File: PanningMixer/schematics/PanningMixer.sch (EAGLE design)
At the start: 67 parts, among them IC1 NE5532D, IC2 NE5532D, IC4 TL047, Q1 BSS84, Q2 BSS123, X1 1503_02

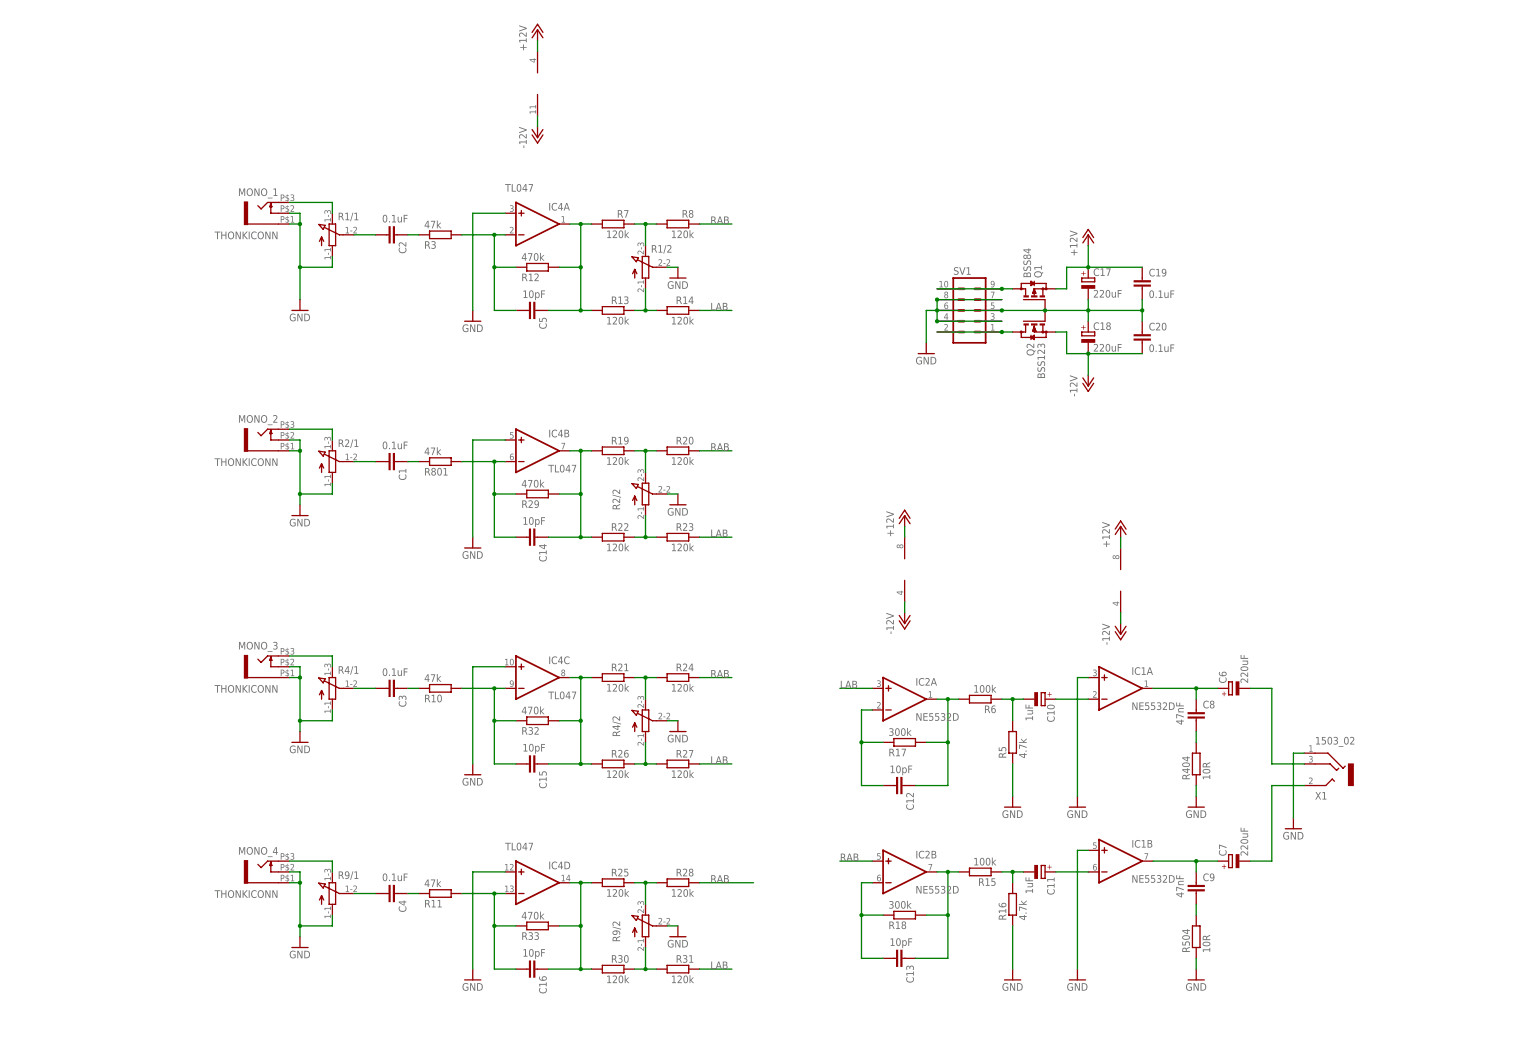
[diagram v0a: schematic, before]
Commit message: Completed placement of components and layout of PCB with no tracking. Added new stereo jack to the Rebel library.
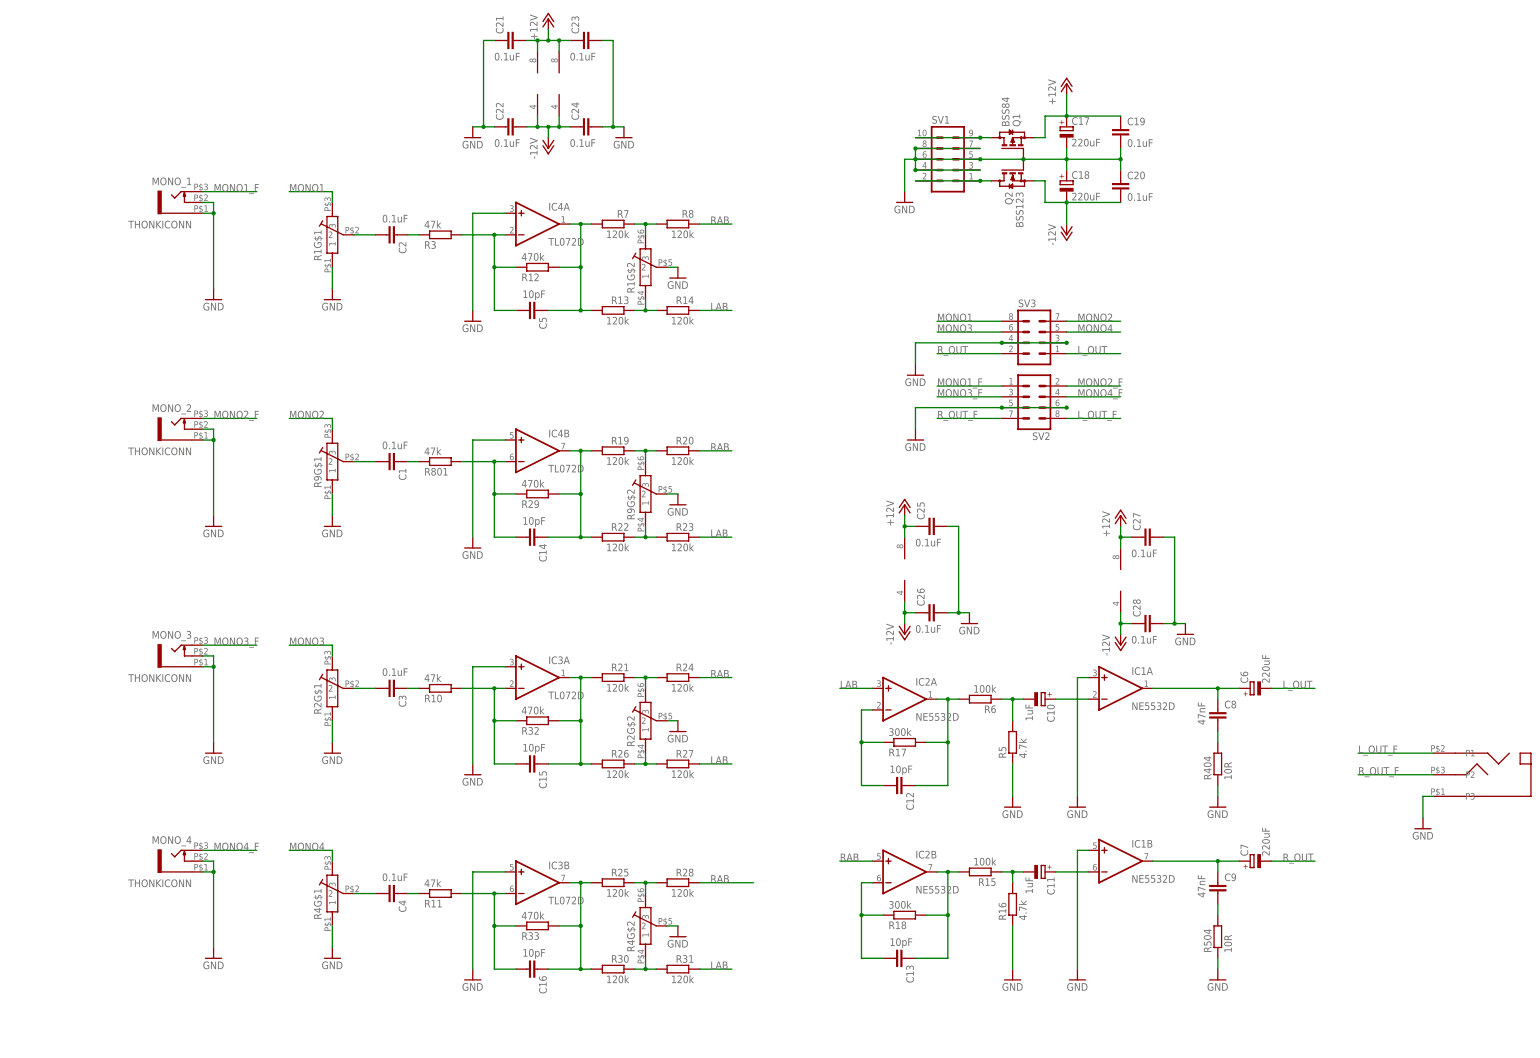
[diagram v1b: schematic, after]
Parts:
- removed X1: 1503_02, con-lumberg:1503_02
- added C21, C22, C23, C24, C25, C26, C27, C28: 0.1uF, Rebel:C-EUC0603
- added IC3: TL072D, linear:TL072D
- added SV2, SV3: (no value), con-lstb:MA04-2
- added U$1: CON-PROSIGNAL_MJ-355W, Rebel:CON-PROSIGNAL_MJ-355W
- IC4: value TL047 -> TL072D; device adafruit:QUAD_OPAMPD -> linear:TL072D
- R1, R2, R4, R9: value (none) -> POT-ALPHA_DUAL_9MM; device pot:3RP/1610G -> Rebel:POT-ALPHA_DUAL_9MM
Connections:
- removed net N$15: MONO_2.3, R2/1.E
- removed net N$2: MONO_4.3, R9/1.E
- removed net N$25: C7.-, X1.2
- removed net N$26: C6.-, X1.3
- removed net N$4: MONO_1.3, R1/1.E
- removed net N$6: MONO_3.3, R4/1.E
- new net GND_A: MONO_1.4, MONO_1.5, MONO_2.4, MONO_2.5, MONO_3.4, MONO_3.5, MONO_4.4, MONO_4.5, SV2.5, SV2.6, U$1.P3
- new net L_OUT: C6.-, SV3.1
- new net L_OUT_F: SV2.8, U$1.P1
- new net MONO1: R1G$1.3, SV3.8
- new net MONO1_F: MONO_1.3, SV2.1
- new net MONO2: R9G$1.3, SV3.7
- new net MONO2_F: MONO_2.3, SV2.2
- new net MONO3: R2G$1.3, SV3.6
- new net MONO3_F: MONO_3.3, SV2.3
- new net MONO4: R4G$1.3, SV3.5
- new net MONO4_F: MONO_4.3, SV2.4
- new net N$27: R9G$1.1
- new net R_OUT: C7.-, SV3.2
- new net R_OUT_F: SV2.7, U$1.P2
- net +12V: now also C21.2, C23.1, C25.1, C27.1, IC3P.V+
- net -12V: now also C22.2, C24.1, C26.1, C28.1, IC3P.V-
- net GND: now also C21.1, C22.1, C23.2, C24.2, C25.2, C26.2, C27.2, C28.2, IC3A.+IN, IC3B.+IN, R1G$1.1, R1G$2.2, R2G$1.1, R2G$2.2, R4G$1.1, R4G$2.2, R9G$2.2, SV3.3, SV3.4; no longer IC4C.+IN, IC4D.+IN, MONO_1.4, MONO_1.5, MONO_2.4, MONO_2.5, MONO_3.4, MONO_3.5, MONO_4.4, MONO_4.5, R1/1.A, R1/2.S, R2/1.A, R2/2.S, R4/1.A, R4/2.S, R9/1.A, R9/2.S, X1.1
- net N$10: now also R9G$1.2; no longer R2/1.S
- net N$11: now also R1G$1.2; no longer R1/1.S
- net N$14: now also R1G$2.3; no longer R1/2.E
- net N$16: now also R4G$1.2; no longer R9/1.S
- net N$19: now also R2G$1.2; no longer R4/1.S
- net N$24: now also R1G$2.1; no longer R1/2.A
- net N$33: now also R9G$2.3; no longer R2/2.E
- net N$35: now also R9G$2.1; no longer R2/2.A
- net N$36: now also R2G$2.3; no longer R4/2.E
- net N$37: now also IC3A.OUT; no longer IC4C.OUT
- net N$38: now also R2G$2.1; no longer R4/2.A
- net N$39: now also R4G$2.3; no longer R9/2.E
- net N$40: now also IC3B.OUT; no longer IC4D.OUT
- net N$41: now also R4G$2.1; no longer R9/2.A
- net N$45: now also IC3A.-IN; no longer IC4C.-IN
- net N$47: now also IC3B.-IN; no longer IC4D.-IN
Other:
- moved on the sheet: C17, C18, C19, C20, C6, C7, C8, C9, MONO_1, MONO_2, MONO_3, MONO_4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

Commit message: Synced missed Panning Mixer.sch file from
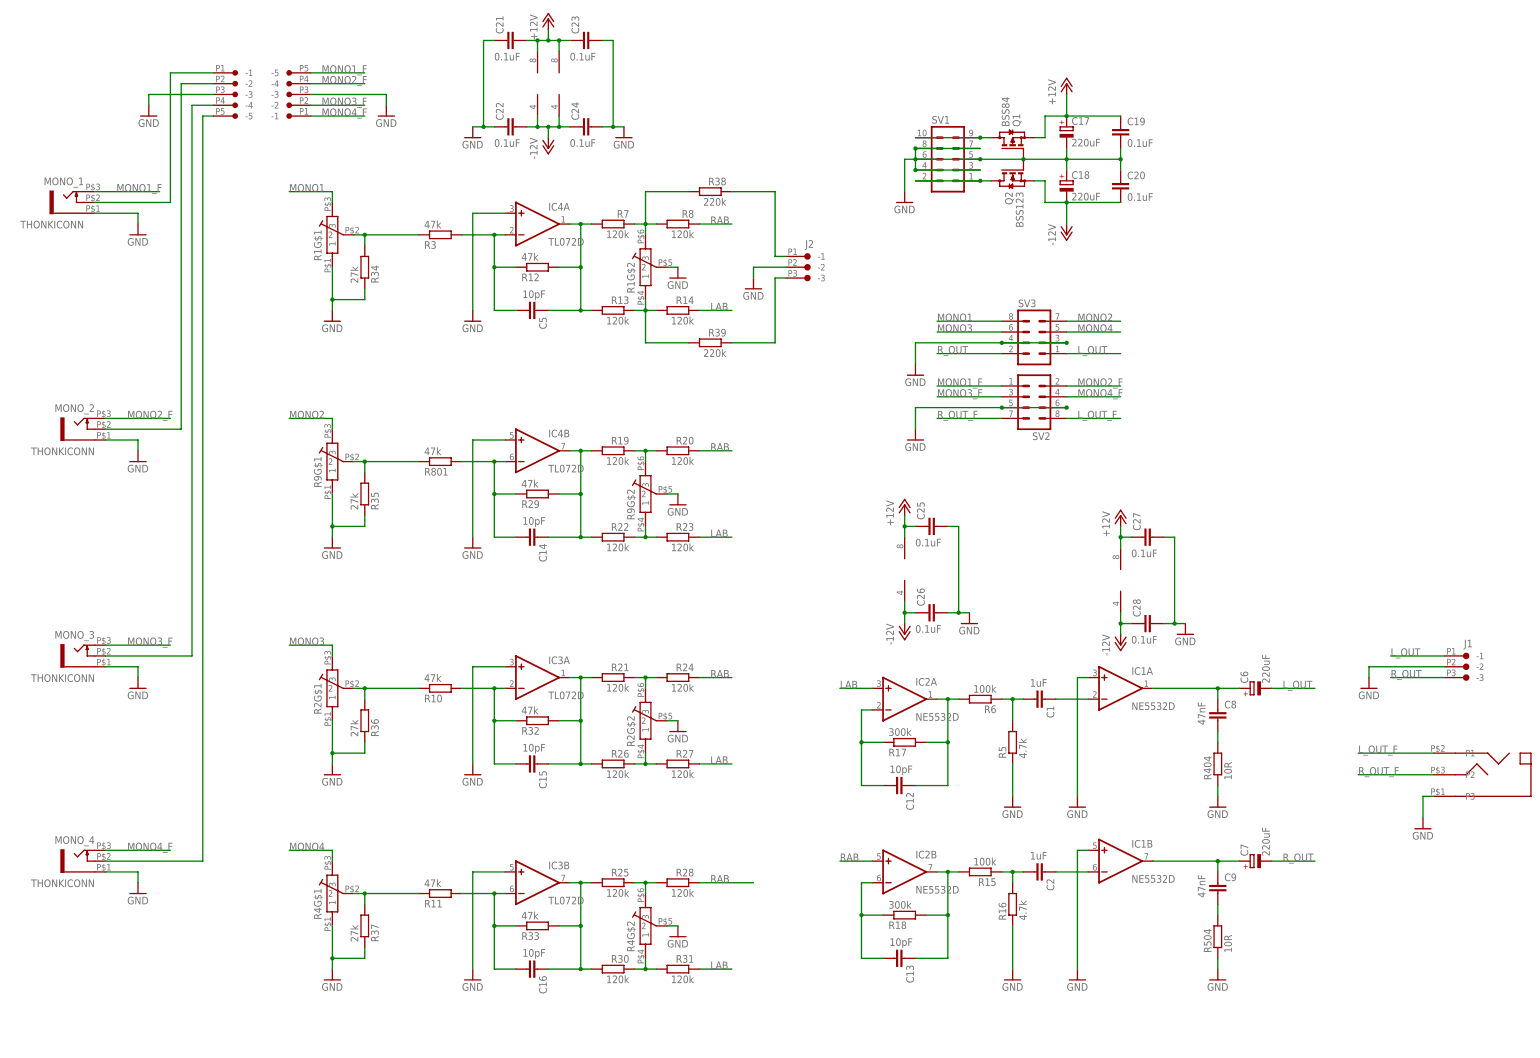
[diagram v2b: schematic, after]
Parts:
- removed C10, C11: 1uF, rcl:CPOL-EUA
- removed C3, C4: 0.1uF, Rebel:C-EUC0603
- added J1, J2: CON-JST_PH_3W, Rebel:CON-JST_PH_3W
- added R34, R35, R36, R37: 27k, Rebel:R-EU_0603
- added R38, R39: 220k, Rebel:R-EU_0603
- added U$2, U$4: CON-JST_PH_5W, Rebel:CON-JST_PH_5W
- C1, C2: value 0.1uF -> 1uF; device Rebel:C-EUC0603 -> Rebel:C-EUC1210
- R12, R29, R32, R33: value 470k -> 47k
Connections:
- removed net N$19: C3.2, R2G$1.2
- removed net N$20: C3.1, R10.1
- removed net N$27: R9G$1.1
- new net N$15: MONO_4.4, U$2.-5
- new net N$2: MONO_2.4, U$2.-2
- new net N$4: MONO_1.4, U$2.-1
- new net N$6: MONO_3.4, U$2.-4
- net GND: now also J1.-2, J2.-2, MONO_4.5, R34.1, R35.1, R36.1, R37.1, R9G$1.1
- net GND_A: now also U$2.-3, U$4.-3; no longer MONO_1.4, MONO_2.4, MONO_3.4, MONO_4.4, MONO_4.5
- net L_OUT: now also J1.-1
- net MONO1_F: now also U$4.-5
- net MONO2_F: now also U$4.-4
- net MONO3_F: now also U$4.-2
- net MONO4_F: now also U$4.-1
- net N$1: now also R11.1, R37.2, R4G$1.2; no longer C1.1, R801.1
- net N$10: now also R10.1, R2G$1.2, R36.2; no longer C1.2, R9G$1.2
- net N$11: now also R35.2, R801.1, R9G$1.2; no longer C2.2, R1G$1.2
- net N$14: now also J2.-1, R38.1; no longer R1G$2.3, R7.1, R8.2
- net N$16: now also R13.1, R14.2, R1G$2.1, R39.2; no longer C4.2, R4G$1.2
- net N$17: now also R1G$2.3, R38.2, R7.1, R8.2; no longer C4.1, R11.1
- net N$24: now also J2.-3, R39.1; no longer R13.1, R14.2, R1G$2.1
- net N$28: now also C1.1; no longer C10.+
- net N$29: now also C2.1; no longer C11.+
- net N$5: now also C2.2; no longer C11.-
- net N$7: now also C1.2; no longer C10.-
- net N$8: now also R1G$1.2, R34.2; no longer C2.1
- net R_OUT: now also J1.-3
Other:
- moved on the sheet: C1, C2, MONO_1, MONO_2, MONO_3, MONO_4

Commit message: changed bus headers
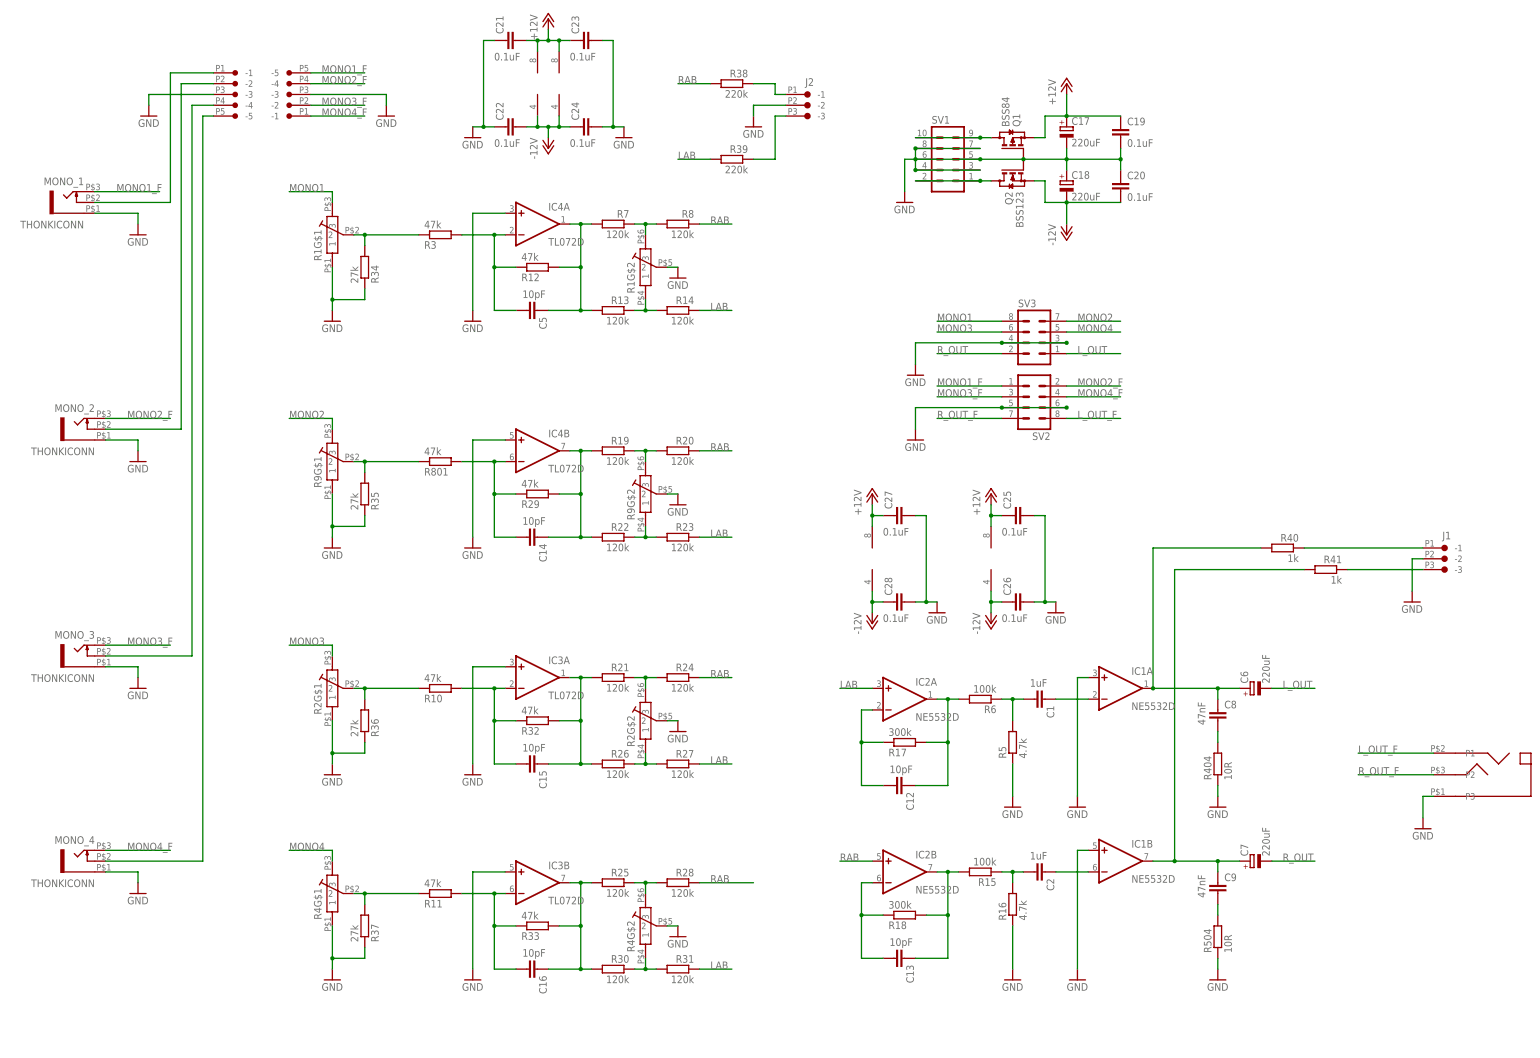
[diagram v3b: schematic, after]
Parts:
- added R40, R41: 1k, Rebel:R-EU_0603
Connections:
- new net N$19: R1G$2.3, R7.1, R8.2
- new net N$20: J1.-3, R41.1
- net LAB: now also R39.2
- net L_OUT: no longer J1.-1
- net N$16: now also J1.-1, R40.1; no longer R13.1, R14.2, R1G$2.1, R39.2
- net N$17: now also R13.1, R14.2, R1G$2.1; no longer R1G$2.3, R38.2, R7.1, R8.2
- net N$22: now also R40.2
- net N$3: now also R41.2
- net RAB: now also R38.2
- net R_OUT: no longer J1.-3
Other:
- moved on the sheet: C25, C26, C27, C28, J1, J2, R38, R39

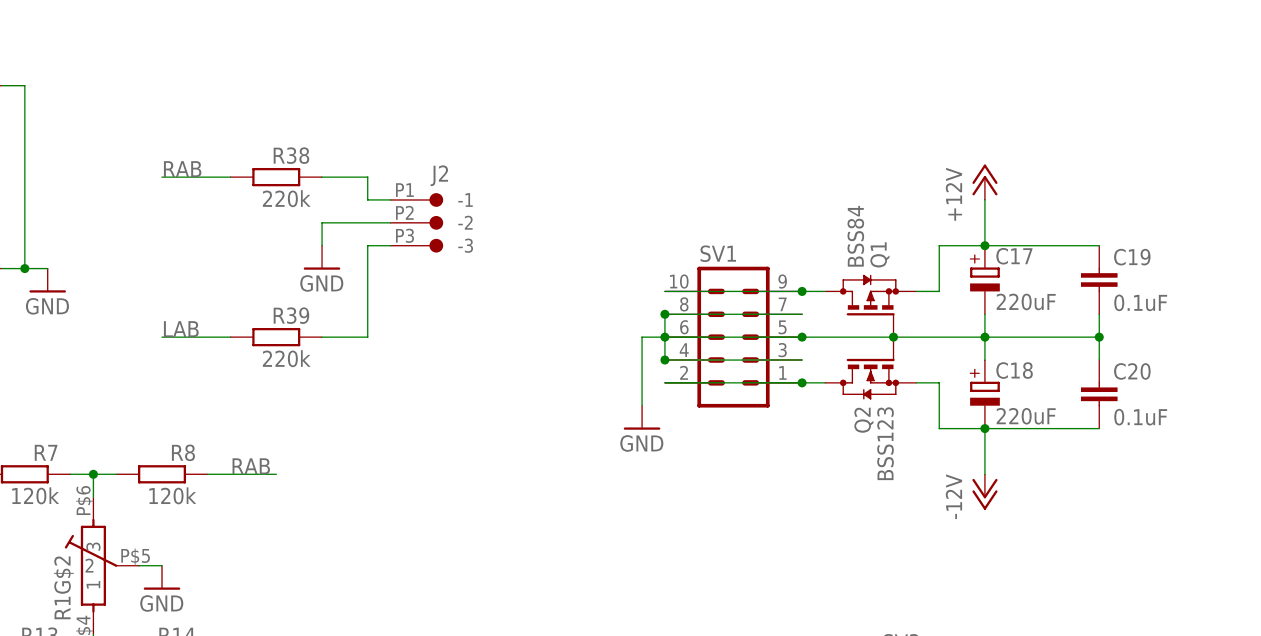
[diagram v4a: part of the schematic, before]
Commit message: Completed layout and tracking for Panning Mixer Rev 1
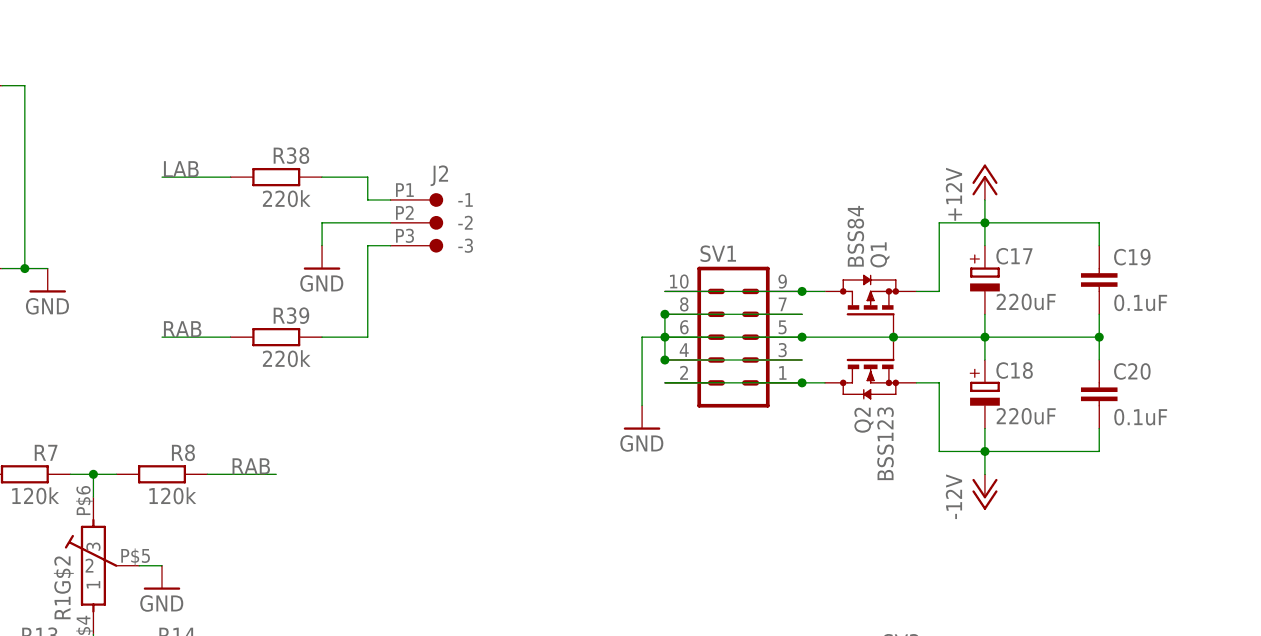
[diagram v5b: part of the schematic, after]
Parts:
- renumbered U$1 to U1, U$2 to U2, U$4 to U4
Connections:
- net GND: no longer MONO_4.5
- net GND_A: now also MONO_4.5
- net LAB: now also R38.2; no longer R39.2
- net RAB: now also R39.2; no longer R38.2
